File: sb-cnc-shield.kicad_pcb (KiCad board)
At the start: 2 copper layers, 68.6 x 53.3 mm, 63 parts, among them P1 XMOT, P2 YMOT, P3 ZMOT, P4 AMOT, P5 UART, P6 I2C, P7 ES_SETUP, P8 VMOT, SW1 RESET, U1 ARDUINO_UNO_SHIELD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

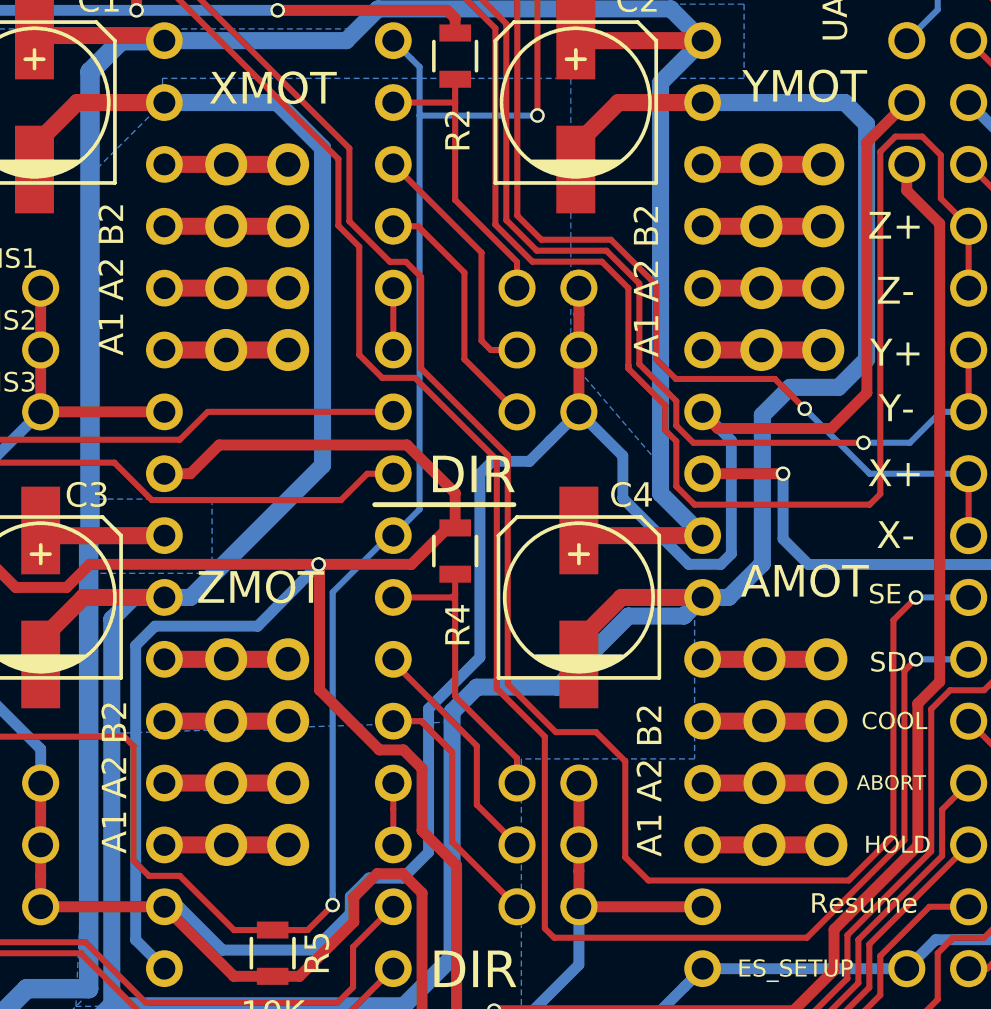
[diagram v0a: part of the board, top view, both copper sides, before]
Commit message: - changed width of tracks to motors, from 0.7 to 1.5 - add tracks to motors on down side
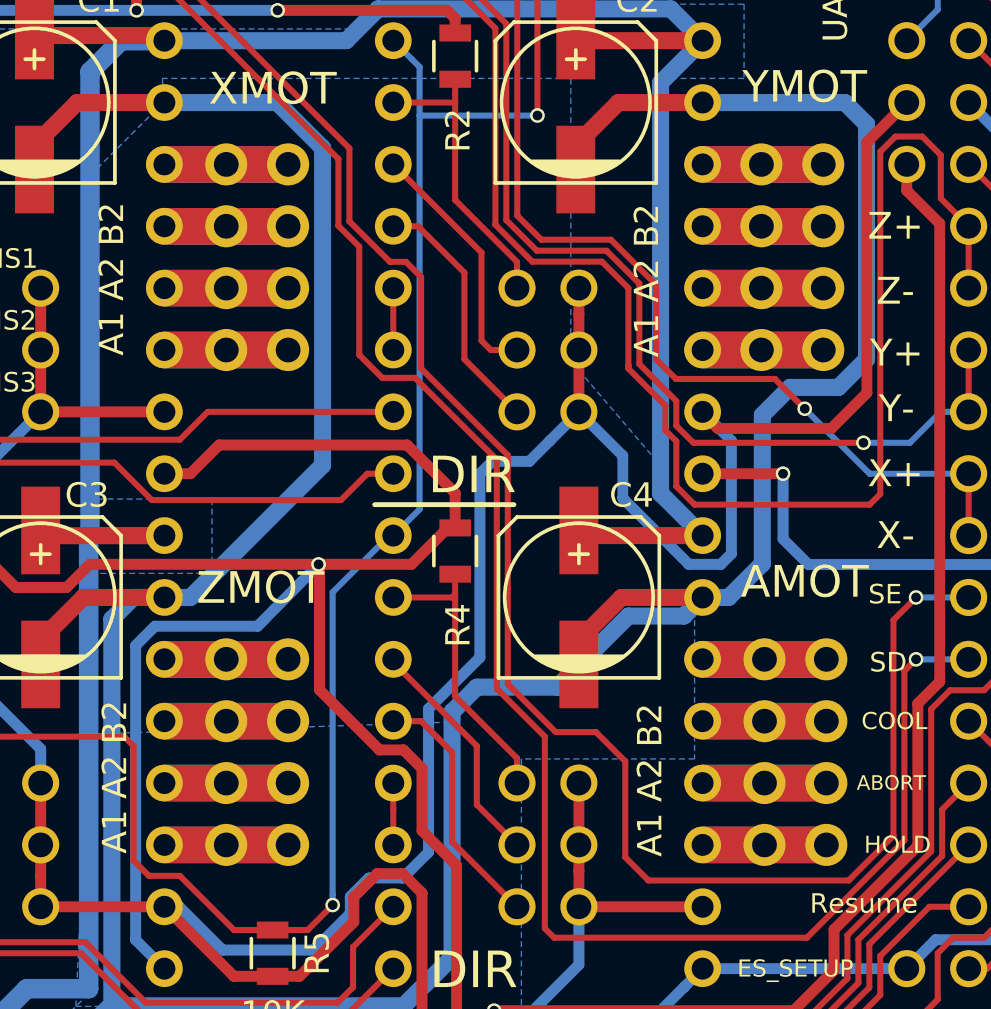
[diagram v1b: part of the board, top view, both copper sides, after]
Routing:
- net Net-(P4-Pad4): track 5.08 -> 10.2 mm
- net Net-(P4-Pad3): track 5.08 -> 10.2 mm
- net Net-(P4-Pad2): track 5.08 -> 10.2 mm
- net Net-(P4-Pad1): track 5.08 -> 10.2 mm
- net Net-(P3-Pad4): track 5.08 -> 10.2 mm
- net Net-(P3-Pad3): track 5.08 -> 10.2 mm
- net Net-(P3-Pad2): track 5.08 -> 10.2 mm
- net Net-(P3-Pad1): track 5.08 -> 10.2 mm
- net Net-(P1-Pad4): track 5.08 -> 10.2 mm
- net Net-(P1-Pad3): track 5.08 -> 10.2 mm
- net Net-(P1-Pad2): track 5.08 -> 10.2 mm
- net Net-(P1-Pad1): track 5.08 -> 10.2 mm
- net Net-(P2-Pad4): track 4.95 -> 9.91 mm
- net Net-(P2-Pad3): track 4.95 -> 9.91 mm
- net Net-(P2-Pad2): track 4.95 -> 9.91 mm
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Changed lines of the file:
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@@
-(kicad_pcb (version 4) (host pcbnew 4.0.2-stable)
+(kicad_pcb (version 4) (host pcbnew 4.0.3-stable)
   (general
     (links 174)
     (no_connects 0)
-    (area 94.030667 58.110001 189.306334 124.8608)
+    (area 114.249999 65.989999 182.930001 119.430001)
     (thickness 1.6)
     (drawings 33)
-    (tracks 788)
+    (tracks 804)
     (zones 0)
     (modules 63)
@@
   (segment (start 153.543 104.775) (end 153.543 105.842731) (width 0.25) (layer F.Cu) (net 5))
   (segment (start 153.543 105.842731) (end 153.543 107.315) (width 0.25) (layer F.Cu) (net 5))
-  (segment (start 149.225 79.375) (end 146.685 79.375) (width 0.7) (layer F.Cu) (net 6))
-  (segment (start 144.145 79.375) (end 146.685 79.375) (width 0.7) (layer F.Cu) (net 6))
-  (segment (start 149.225 81.915) (end 146.685 81.915) (width 0.7) (layer F.Cu) (net 7))
-  (segment (start 144.145 81.915) (end 146.685 81.915) (width 0.7) (layer F.Cu) (net 7))
-  (segment (start 149.225 84.455) (end 146.685 84.455) (width 0.7) (layer F.Cu) (net 8))
-  (segment (start 144.145 84.455) (end 146.685 84.455) (width 0.7) (layer F.Cu) (net 8))
-  (segment (start 149.225 86.995) (end 146.685 86.995) (width 0.7) (layer F.Cu) (net 9))
-  (segment (start 144.145 86.995) (end 146.685 86.995) (width 0.7) (layer F.Cu) (net 9))
-  (segment (start 168.656 79.375) (end 171.196 79.375) (width 0.7) (layer F.Cu) (net 10))
-  (segment (start 166.243 79.375) (end 168.656 79.375) (width 0.7) (layer F.Cu) (net 10))
-  (segment (start 168.656 81.915) (end 171.196 81.915) (width 0.7) (layer F.Cu) (net 11))
-  (segment (start 166.243 81.915) (end 168.656 81.915) (width 0.7) (layer F.Cu) (net 11))
-  (segment (start 168.656 84.455) (end 171.196 84.455) (width 0.7) (layer F.Cu) (net 12))
-  (segment (start 166.243 84.455) (end 168.656 84.455) (width 0.7) (layer F.Cu) (net 12))
-  (segment (start 168.656 86.995) (end 171.196 86.995) (width 0.7) (layer F.Cu) (net 13))
-  (segment (start 166.243 86.995) (end 168.656 86.995) (width 0.7) (layer F.Cu) (net 13))
-  (segment (start 149.225 99.695) (end 146.685 99.695) (width 0.7) (layer F.Cu) (net 14))
-  (segment (start 144.145 99.695) (end 146.685 99.695) (width 0.7) (layer F.Cu) (net 14))
-  (segment (start 149.225 102.235) (end 146.685 102.235) (width 0.7) (layer F.Cu) (net 15))
-  (segment (start 144.145 102.235) (end 146.685 102.235) (width 0.7) (layer F.Cu) (net 15))
-  (segment (start 146.685 104.775) (end 149.225 104.775) (width 0.7) (layer F.Cu) (net 16))
-  (segment (start 144.145 104.775) (end 146.685 104.775) (width 0.7) (layer F.Cu) (net 16))
-  (segment (start 149.225 107.315) (end 146.685 107.315) (width 0.7) (layer F.Cu) (net 17))
-  (segment (start 144.145 107.315) (end 146.685 107.315) (width 0.7) (layer F.Cu) (net 17))
-  (segment (start 171.323 99.695) (end 168.783 99.695) (width 0.7) (layer F.Cu) (net 18))
-  (segment (start 166.243 99.695) (end 168.783 99.695) (width 0.7) (layer F.Cu) (net 18))
-  (segment (start 168.783 102.235) (end 171.323 102.235) (width 0.7) (layer F.Cu) (net 19))
-  (segment (start 166.243 102.235) (end 168.783 102.235) (width 0.7) (layer F.Cu) (net 19))
-  (segment (start 168.783 104.775) (end 171.323 104.775) (width 0.7) (layer F.Cu) (net 20))
-  (segment (start 166.243 104.775) (end 168.783 104.775) (width 0.7) (layer F.Cu) (net 20))
-  (segment (start 168.783 107.315) (end 171.323 107.315) (width 0.7) (layer F.Cu) (net 21))
-  (segment (start 166.243 107.315) (end 168.783 107.315) (width 0.7) (layer F.Cu) (net 21))
+  (segment (start 144.145 79.375) (end 146.685 79.375) (width 1.5) (layer B.Cu) (net 6))
+  (segment (start 144.145 79.375) (end 149.225 79.375) (width 1.5) (layer F.Cu) (net 6))
+  (segment (start 149.225 79.375) (end 146.685 79.375) (width 1.5) (layer B.Cu) (net 6))
+  (segment (start 144.145 81.915) (end 149.225 81.915) (width 1.5) (layer F.Cu) (net 7))
+  (segment (start 149.225 81.915) (end 146.685 81.915) (width 1.5) (layer B.Cu) (net 7))
+  (segment (start 144.145 81.915) (end 146.685 81.915) (width 1.5) (layer B.Cu) (net 7))
+  (segment (start 144.145 84.455) (end 149.225 84.455) (width 1.5) (layer F.Cu) (net 8))
+  (segment (start 149.225 84.455) (end 146.685 84.455) (width 1.5) (layer B.Cu) (net 8))
+  (segment (start 144.145 84.455) (end 146.685 84.455) (width 1.5) (layer B.Cu) (net 8))
+  (segment (start 144.145 86.995) (end 149.225 86.995) (width 1.5) (layer F.Cu) (net 9))
+  (segment (start 149.225 86.995) (end 146.685 86.995) (width 1.5) (layer B.Cu) (net 9))
+  (segment (start 144.145 86.995) (end 146.685 86.995) (width 1.5) (layer B.Cu) (net 9))
+  (segment (start 166.243 79.375) (end 171.196 79.375) (width 1.5) (layer F.Cu) (net 10))
+  (segment (start 168.656 79.375) (end 171.196 79.375) (width 1.5) (layer B.Cu) (net 10))
+  (segment (start 166.243 79.375) (end 168.656 79.375) (width 1.5) (layer B.Cu) (net 10))
+  (segment (start 166.243 81.915) (end 171.196 81.915) (width 1.5) (layer F.Cu) (net 11))
+  (segment (start 168.656 81.915) (end 171.196 81.915) (width 1.5) (layer B.Cu) (net 11))
+  (segment (start 166.243 81.915) (end 168.656 81.915) (width 1.5) (layer B.Cu) (net 11))
+  (segment (start 166.243 84.455) (end 171.196 84.455) (width 1.5) (layer F.Cu) (net 12))
+  (segment (start 168.656 84.455) (end 171.196 84.455) (width 1.5) (layer B.Cu) (net 12))
+  (segment (start 166.243 84.455) (end 168.656 84.455) (width 1.5) (layer B.Cu) (net 12))
+  (segment (start 166.243 86.995) (end 171.196 86.995) (width 1.5) (layer F.Cu) (net 13))
+  (segment (start 168.656 86.995) (end 171.196 86.995) (width 1.5) (layer B.Cu) (net 13))
+  (segment (start 166.243 86.995) (end 168.656 86.995) (width 1.5) (layer B.Cu) (net 13))
+  (segment (start 144.145 99.695) (end 149.225 99.695) (width 1.5) (layer F.Cu) (net 14))
+  (segment (start 149.225 99.695) (end 146.685 99.695) (width 1.5) (layer B.Cu) (net 14))
+  (segment (start 144.145 99.695) (end 146.685 99.695) (width 1.5) (layer B.Cu) (net 14))
+  (segment (start 144.145 102.235) (end 149.225 102.235) (width 1.5) (layer F.Cu) (net 15))
+  (segment (start 149.225 102.235) (end 146.685 102.235) (width 1.5) (layer B.Cu) (net 15))
+  (segment (start 144.145 102.235) (end 146.685 102.235) (width 1.5) (layer B.Cu) (net 15))
+  (segment (start 144.145 104.775) (end 149.225 104.775) (width 1.5) (layer F.Cu) (net 16))
+  (segment (start 146.685 104.775) (end 149.225 104.775) (width 1.5) (layer B.Cu) (net 16))
+  (segment (start 144.145 104.775) (end 146.685 104.775) (width 1.5) (layer B.Cu) (net 16))
+  (segment (start 144.145 107.315) (end 149.225 107.315) (width 1.5) (layer F.Cu) (net 17))
+  (segment (start 149.225 107.315) (end 146.685 107.315) (width 1.5) (layer B.Cu) (net 17))
+  (segment (start 144.145 107.315) (end 146.685 107.315) (width 1.5) (layer B.Cu) (net 17))
+  (segment (start 166.243 99.695) (end 171.323 99.695) (width 1.5) (layer F.Cu) (net 18))
+  (segment (start 171.323 99.695) (end 168.783 99.695) (width 1.5) (layer B.Cu) (net 18))
+  (segment (start 166.243 99.695) (end 168.783 99.695) (width 1.5) (layer B.Cu) (net 18))
+  (segment (start 166.243 102.235) (end 171.323 102.235) (width 1.5) (layer F.Cu) (net 19))
+  (segment (start 168.783 102.235) (end 171.323 102.235) (width 1.5) (layer B.Cu) (net 19))
+  (segment (start 166.243 102.235) (end 168.783 102.235) (width 1.5) (layer B.Cu) (net 19))
+  (segment (start 166.243 104.775) (end 171.323 104.775) (width 1.5) (layer F.Cu) (net 20))
+  (segment (start 168.783 104.775) (end 171.323 104.775) (width 1.5) (layer B.Cu) (net 20))
+  (segment (start 166.243 104.775) (end 168.783 104.775) (width 1.5) (layer B.Cu) (net 20))
+  (segment (start 166.243 107.315) (end 171.323 107.315) (width 1.5) (layer F.Cu) (net 21))
+  (segment (start 168.783 107.315) (end 171.323 107.315) (width 1.5) (layer B.Cu) (net 21))
+  (segment (start 166.243 107.315) (end 168.783 107.315) (width 1.5) (layer B.Cu) (net 21))
   (segment (start 144.145 109.855) (end 144.7546 109.855) (width 0.45) (layer B.Cu) (net 22))
   (segment (start 144.7546 109.855) (end 146.5326 111.633) (width 0.45) (layer B.Cu) (net 22))
@@
         (xy 138.4808 116.9924) (xy 141.5288 113.9444) (xy 140.5128 113.9444) (xy 141.0208 102.7684) (xy 155.7528 102.277333)
         (xy 155.7528 101.7524) (xy 156.7688 100.7364) (xy 160.3248 100.7364) (xy 163.3728 97.6884) (xy 165.9128 97.6884)
-        (xy 165.9128 103.7844)
       )
     )
